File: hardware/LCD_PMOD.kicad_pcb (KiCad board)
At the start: 2 copper layers, 175.3 x 95.2 mm, 170 parts, among them IC1 TPS61169DCKR, IC2 TPD4E001DRLR, IC3 AR1021-I/SS, IC4 M24C32-WMN6P, J1 20-pin power socket, J10 OS0, J11 OS1, J12 OS2, J13 PAR, J14 RANGE, J15 REF, J16 MDD01, J17 FTDI, J18 Conn_01x10, J2 VS_SCL, J3 28-pin module socket, J4 691327310016, J5 691327310016, J6 HS_SDA, J7 JMP_A0, J8 DE_IRQ, J9 DIB_V2, U1 ADS8586S, U2 REF5025AD, U3 DS90CF364AMTD, U4 DS90CF36B, U5 MC78L05_SO8, U6 THS4032ID, U7 THS4551IDGKT, U8 THS4551IDGKT, U9 MC79L05_SO8

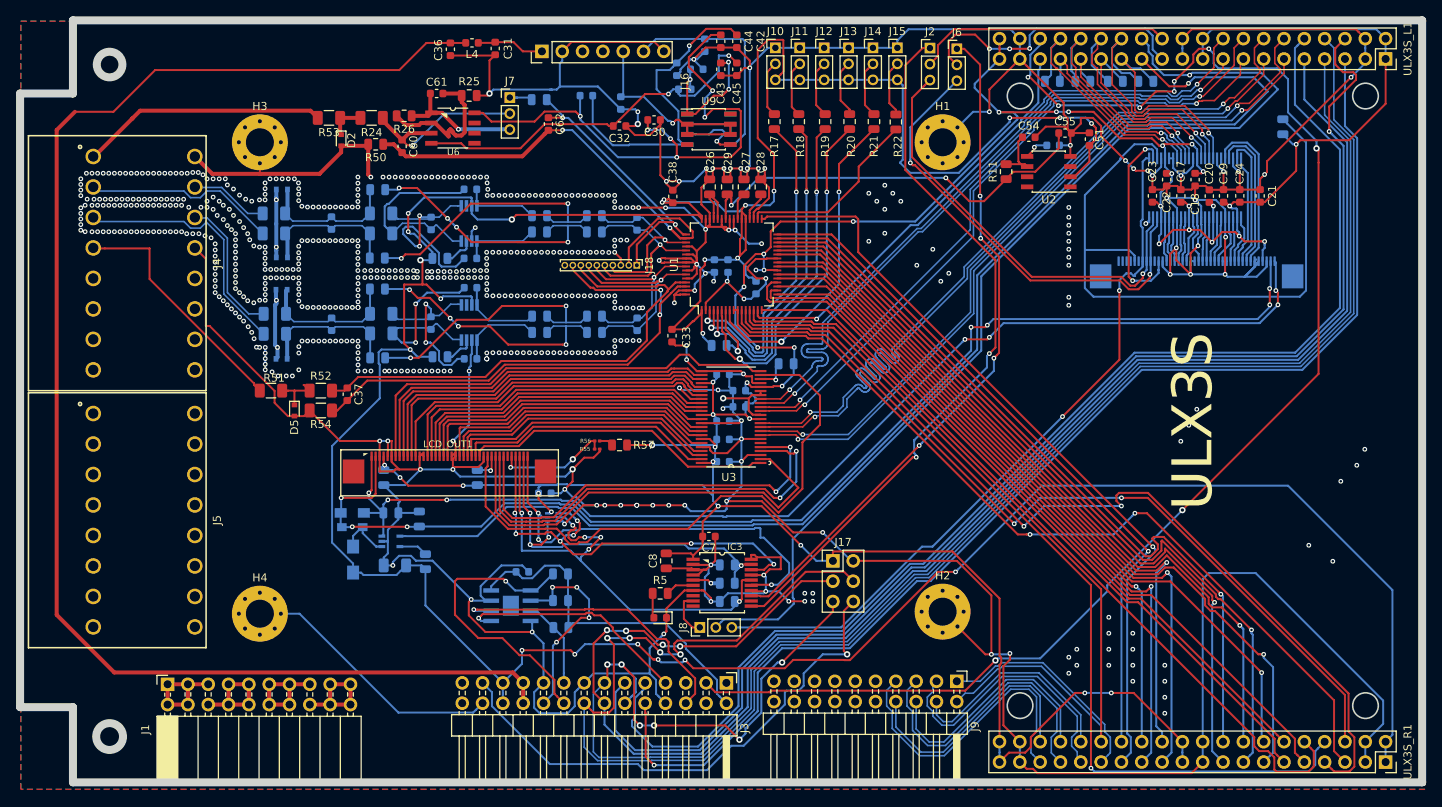
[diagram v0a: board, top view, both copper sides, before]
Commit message: Rerouting
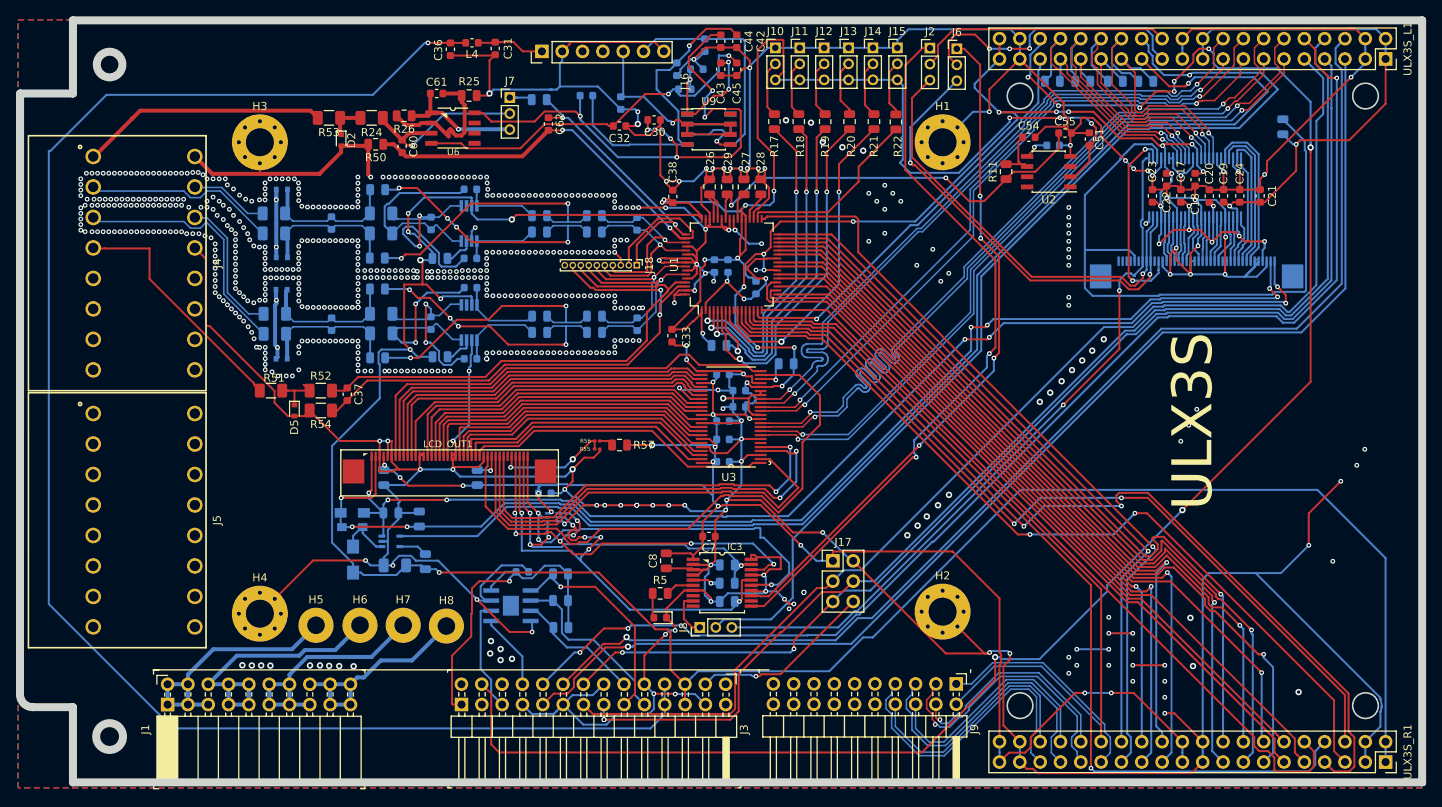
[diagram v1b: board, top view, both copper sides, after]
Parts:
- added H5: OUT+, MountingHole:MountingHole_2.2mm_M2_Pad, F.Cu at (94.9, 116.0)
- added H6: IN+, MountingHole:MountingHole_2.2mm_M2_Pad, F.Cu at (100.4, 116.0)
- added H7: IN-, MountingHole:MountingHole_2.2mm_M2_Pad, F.Cu at (105.8, 116.0)
- added H8: OUT-, MountingHole:MountingHole_2.2mm_M2_Pad, F.Cu at (111.2, 116.1)
- J1: footprint Connector_PinSocket_2.54mm:PinSocket_2x10_P2.54mm_Horizontal -> DIB_V1:PinSocket_2x10_P2.54mm_Horizontal_DIB_V1
- J3: footprint Connector_PinHeader_2.54mm:PinHeader_2x14_P2.54mm_Horizontal -> DIB_V1:PinHeader_2x14_P2.54mm_Horizontal_DIB_V1
- moved J9 0.34 mm to (174.9, 123.3)
- moved J3 0.18 mm to (146.2, 123.4)
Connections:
- J3 pad 1: (no net) -> DIB_+3V3
- J3 pad 10: 0N -> 2P
- J3 pad 11: 0P -> GND
- J3 pad 12: GND -> 0P
- J3 pad 13: 1N -> 2N
- J3 pad 14: 2N -> 1N
- J3 pad 15: GND -> 1P
- J3 pad 16: 1P -> GND
- J3 pad 17: DIB_A2 -> DIB_A0
- J3 pad 18: DIB_A0 -> DIB_A2
- J3 pad 19: GND -> DIB_A1
- J3 pad 2: DIB_+3V3 -> (no net)
- J3 pad 20: DIB_A1 -> GND
- J3 pad 25: DIB_BOOT -> GND
- J3 pad 26: GND -> DIB_BOOT
- J3 pad 3: 13P -> (no net)
- J3 pad 4: (no net) -> 13P
- J3 pad 5: (no net) -> DIB_SCL
- J3 pad 6: DIB_SCL -> (no net)
- J3 pad 7: DIB_SDA -> GND
- J3 pad 8: GND -> DIB_SDA
- J3 pad 9: 2P -> 0N
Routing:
- net 1N: track 211.4 -> 143.7 mm, vias 6 -> 2
- net 1P: track 216.0 -> 149.8 mm, vias 4 -> 2
- net 2N: track 199.3 -> 147.4 mm, vias 4 -> 0
- net DIB_BOOT: track 66.2 -> 22.9 mm
- net 13P: track 178.6 -> 217.6 mm
- net DIB_SCL: track 37.8 -> 14.1 mm, vias 1 -> 0
- net IN+: track 12.7 -> 34.7 mm
- net +12V: track 180.6 -> 202.3 mm, vias 0 -> 1
- net OUT+: track 12.7 -> 32.5 mm
- net DIB_SDA: track 29.2 -> 9.52 mm, vias 1 -> 0
- net IN-: track 12.7 -> 30.7 mm
- net GND: track 1090.0 -> 1106.9 mm, vias 615 -> 654
- net OUT-: track 12.7 -> 27.7 mm
- net 0P: track 162.4 -> 149.9 mm
- net DIB_A0: track 37.3 -> 27.3 mm
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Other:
- outline, holes or cut-outs redrawn

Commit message: Moving ULX3S connector lower
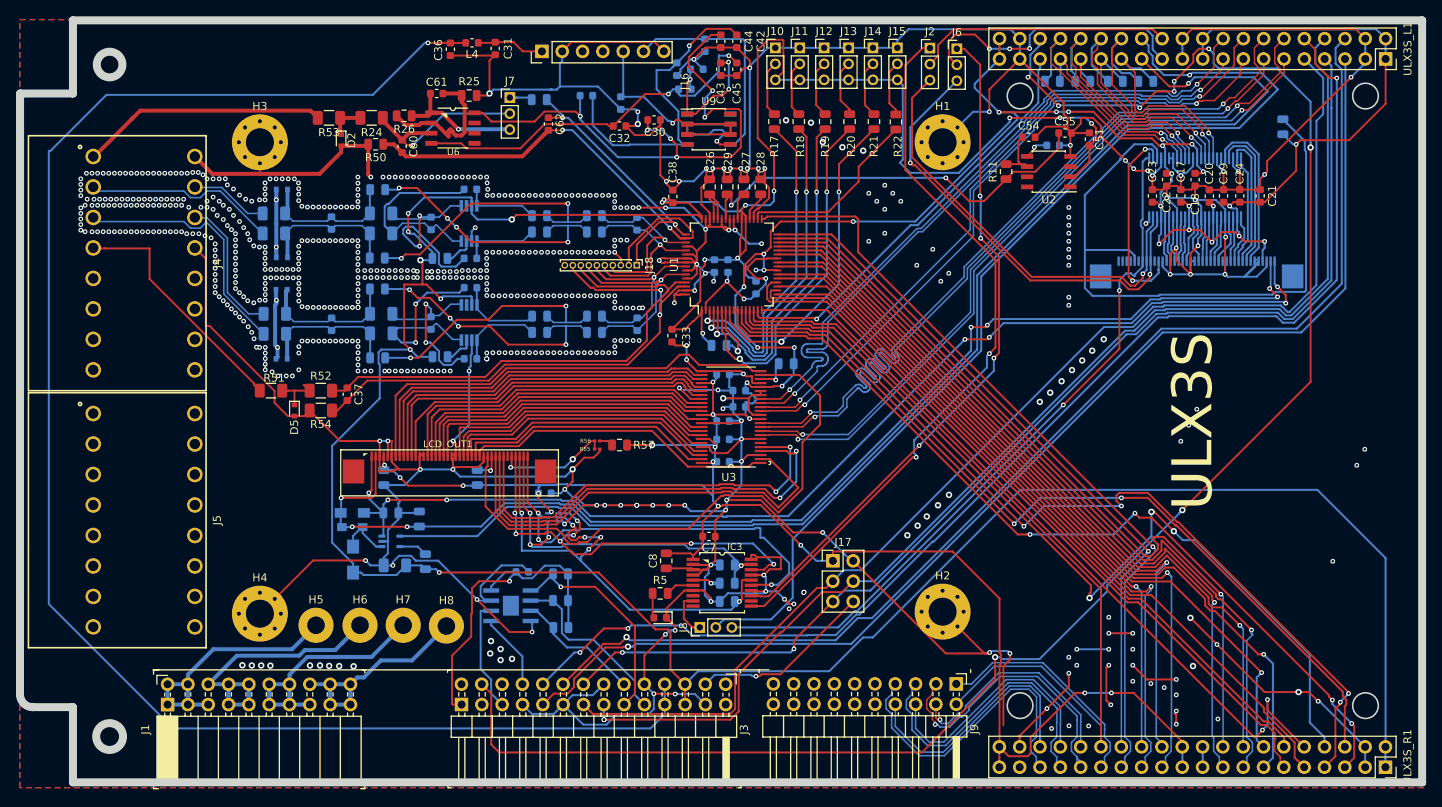
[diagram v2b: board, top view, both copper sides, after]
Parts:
- moved ULX3S_R1 0.64 mm to (228.6, 133.7)
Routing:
- net GND: track 1106.9 -> 1047.1 mm, vias 654 -> 662
- net 26P: track 115.1 -> 111.8 mm, vias 2 -> 4
- net 27P: track 106.8 -> 108.4 mm, vias 2 -> 4
- net 25N: track 98.3 -> 97.0 mm, vias 0 -> 2
- net 17N: track 102.8 -> 104.1 mm
- net 16P: track 35.9 -> 37.2 mm
- net 22P: track 99.3 -> 100.5 mm
- net 24P: track 92.6 -> 93.9 mm
- net 19P: track 85.2 -> 86.4 mm
- net 23N: track 89.9 -> 91.0 mm
- net 24N: track 88.8 -> 89.8 mm
- net 18P: track 97.7 -> 98.5 mm
- net 21N: track 96.2 -> 96.9 mm
- net 3V3: track 438.3 -> 439.0 mm
- net 18N: track 88.0 -> 88.6 mm
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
